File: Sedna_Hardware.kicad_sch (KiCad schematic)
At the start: 51 parts, among them J1 PJ-102A, J10 5-103735-2, J11 2-103634-9, J2 61201021721, J3 PPTC141LFBN-RC, J4 0878340619, J5 5-103634-2, J6 5-103361-1, J7 1935161, J8 1935161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

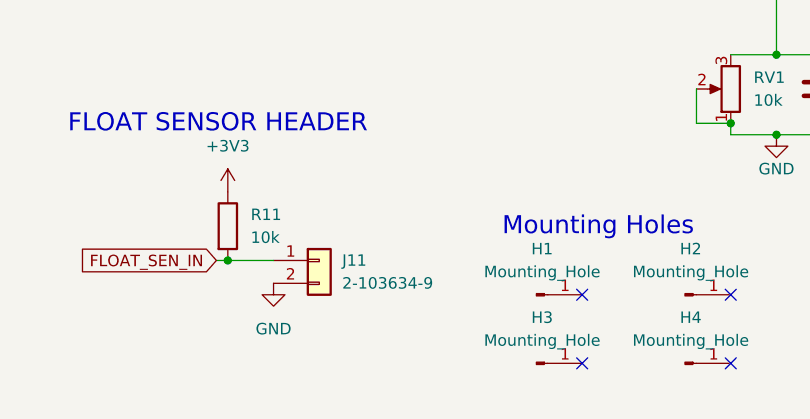
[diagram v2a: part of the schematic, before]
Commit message: placed new header's footpring
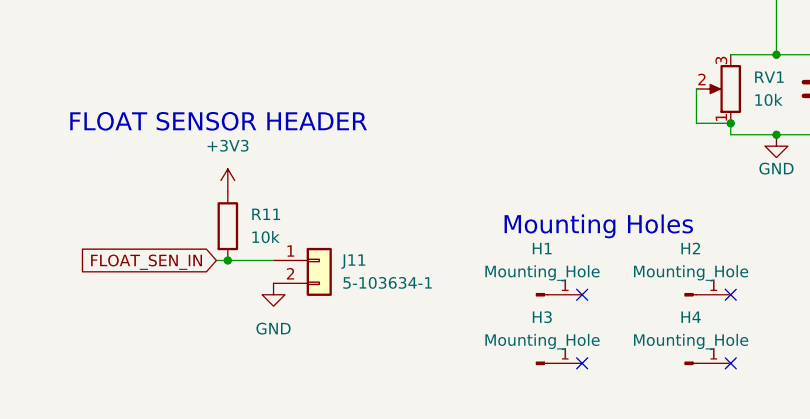
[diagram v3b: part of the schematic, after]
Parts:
- C12: DK_Datasheet_Link https://media.digikey.com/pdf/Data%20Sheets/Panasonic%20Ele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 -> https://www.nichicon.co.jp/english/products/pdfs/e-umt.pdf; DK_Detail_Page https://www.digikey.ca/en/products/detail/panasonic-electro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 -> https://www.digikey.ca/en/products/detail/nichicon/UMT0G470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; Digi-Key_PN P10417TB-ND -> 493-10267-1-ND; MPN ECA-1VM470I -> UMT0G470MDD1TP; Manufacturer Panasonic Electronic Components -> Nichicon
- J10: footprint 5-103634-2:TE_5-103634-2 -> 5-103735-2:MOLEX_1719740003
- J11: value 2-103634-9 -> 5-103634-1; footprint 2-644488-2:TE_2-644488-2 -> 2-103634-9:TE_2-103634-9; DK_Detail_Page https://www.digikey.ca/en/products/detail/te-connectivity-amp-connectors/2-103634-9/1889533 -> https://www.digikey.ca/en/products/detail/te-connectivity-amp-connectors/5-103634-1/1122421; Digi-Key_PN 2-103634-9-ND -> A33857-ND; MPN 2-103634-9 -> 5-103634-1
- J5, J9: footprint 2-644803-3:TE_2-644803-3 -> 5-103634-2:TE_5-103634-2
- J6: footprint 2-644488-3:TE_2-644488-3 -> 5-103361-1:TE_5-103361-1
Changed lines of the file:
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@@
       (effects (font (size 1.27 1.27)) (justify left))
     )
-    (property "Footprint" "2-644803-3:TE_2-644803-3" (id 2) (at 252.73 121.92 0)
+    (property "Footprint" "5-103634-2:TE_5-103634-2" (id 2) (at 252.73 121.92 0)
       (effects (font (size 1.27 1.27)) hide)
     )
@@
       (effects (font (size 1.27 1.27)) (justify left))
     )
-    (property "Value" "2-103634-9" (id 1) (at 109.22 181.6099 0)
-      (effects (font (size 1.27 1.27)) (justify left))
-    )
-    (property "Footprint" "2-644488-2:TE_2-644488-2" (id 2) (at 106.68 179.07 0)
+    (property "Value" "5-103634-1" (id 1) (at 109.22 181.6099 0)
+      (effects (font (size 1.27 1.27)) (justify left))
+    )
+    (property "Footprint" "2-103634-9:TE_2-103634-9" (id 2) (at 106.68 179.07 0)
       (effects (font (size 1.27 1.27)) hide)
     )
@@
       (effects (font (size 1.27 1.27)) hide)
     )
-    (property "Digi-Key_PN" "2-103634-9-ND" (id 4) (at 106.68 179.07 0)
-      (effects (font (size 1.27 1.27)) hide)
-    )
-    (property "MPN" "2-103634-9" (id 5) (at 106.68 179.07 0)
+    (property "Digi-Key_PN" "A33857-ND" (id 4) (at 106.68 179.07 0)
+      (effects (font (size 1.27 1.27)) hide)
+    )
+    (property "MPN" "5-103634-1" (id 5) (at 106.68 179.07 0)
       (effects (font (size 1.27 1.27)) hide)
     )
@@
       (effects (font (size 1.27 1.27)) hide)
     )
-    (property "DK_Detail_Page" "https://www.digikey.ca/en/products/detail/te-connectivity-amp-connectors/2-103634-9/1889533" (id 9) (at 106.68 179.07 0)
+    (property "DK_Detail_Page" "https://www.digikey.ca/en/products/detail/te-connectivity-amp-connectors/5-103634-1/1122421" (id 9) (at 106.68 179.07 0)
       (effects (font (size 1.27 1.27)) hide)
     )
@@
       (effects (font (size 1.27 1.27)) (justify left))
     )
-    (property "Footprint" "2-644803-3:TE_2-644803-3" (id 2) (at 251.46 152.4 0)
+    (property "Footprint" "5-103634-2:TE_5-103634-2" (id 2) (at 251.46 152.4 0)
       (effects (font (size 1.27 1.27)) hide)
     )
@@
     (property "Reference" "J6" (id 0) (at 147.32 116.84 0))
     (property "Value" "5-103361-1" (id 1) (at 147.32 119.38 0))
-    (property "Footprint" "2-644488-3:TE_2-644488-3" (id 2) (at 147.32 125.73 0)
+    (property "Footprint" "5-103361-1:TE_5-103361-1" (id 2) (at 147.32 125.73 0)
       (effects (font (size 1.27 1.27)) hide)
     )
@@
       (effects (font (size 1.27 1.27)) (justify left))
     )
-    (property "Footprint" "5-103634-2:TE_5-103634-2" (id 2) (at 53.34 177.8 0)
+    (property "Footprint" "5-103735-2:MOLEX_1719740003" (id 2) (at 53.34 177.8 0)
       (effects (font (size 1.27 1.27)) hide)
     )
@@
       (effects (font (size 1.27 1.27)) hide)
     )
-    (property "Datasheet" "https://media.digikey.com/pdf/Data%20Sheets/Panasonic%20Electronic%20Components/ECA-xxM%20Series,TypeA.pdf" (id 3) (at 220.98 153.67 0)
-      (effects (font (size 1.27 1.27)) hide)
-    )
-    (property "Digi-Key_PN" "P10417TB-ND" (id 4) (at 220.98 153.67 0)
-      (effects (font (size 1.27 1.27)) hide)
-    )
-    (property "MPN" "ECA-1VM470I" (id 5) (at 220.98 153.67 0)
+    (property "Datasheet" "https://www.nichicon.co.jp/english/products/pdfs/e-umt.pdf" (id 3) (at 220.98 153.67 0)
+      (effects (font (size 1.27 1.27)) hide)
+    )
+    (property "Digi-Key_PN" "493-10267-1-ND" (id 4) (at 220.98 153.67 0)
+      (effects (font (size 1.27 1.27)) hide)
+    )
+    (property "MPN" "UMT0G470MDD1TP" (id 5) (at 220.98 153.67 0)
       (effects (font (size 1.27 1.27)) hide)
     )
@@
       (effects (font (size 1.27 1.27)) hide)
     )
-    (property "DK_Datasheet_Link" "https://media.digikey.com/pdf/Data%20Sheets/Panasonic%20Electronic%20Components/ECA-xxM%20Series,TypeA.pdf" (id 7) (at 220.98 153.67 0)
-      (effects (font (size 1.27 1.27)) hide)
-    )
-    (property "DK_Detail_Page" "https://www.digikey.ca/en/products/detail/panasonic-electronic-components/ECA-1VM470I/268502" (id 8) (at 220.98 153.67 0)
-      (effects (font (size 1.27 1.27)) hide)
-    )
-    (property "Description" "CAP ALUM 47UF 20% 35V RADIAL" (id 9) (at 220.98 153.67 0)
-      (effects (font (size 1.27 1.27)) hide)
-    )
-    (property "Manufacturer" "Panasonic Electronic Components" (id 10) (at 220.98 153.67 0)
+    (property "DK_Datasheet_Link" "https://www.nichicon.co.jp/english/products/pdfs/e-umt.pdf" (id 7) (at 220.98 153.67 0)
+      (effects (font (size 1.27 1.27)) hide)
+    )
+    (property "DK_Detail_Page" "https://www.digikey.ca/en/products/detail/nichicon/UMT0G470MDD1TP/4312526" (id 8) (at 220.98 153.67 0)
+      (effects (font (size 1.27 1.27)) hide)
+    )
+    (property "Description" "47 µF 4 V Aluminum Electrolytic Capacitors Radial, Can - 1000 Hrs @ 105°C" (id 9) (at 220.98 153.67 0)
+      (effects (font (size 1.27 1.27)) hide)
+    )
+    (property "Manufacturer" "Nichicon" (id 10) (at 220.98 153.67 0)
       (effects (font (size 1.27 1.27)) hide)
     )
@@
     )
     (path "/2f024473-bb01-40b1-8417-7bc91aef9781"
-      (reference "J5") (unit 1) (value "5-103634-2") (footprint "2-644803-3:TE_2-644803-3")
+      (reference "J5") (unit 1) (value "5-103634-2") (footprint "5-103634-2:TE_5-103634-2")
     )
     (path "/475ad85a-f040-4464-8a55-a263ba5a9f31"
-      (reference "J6") (unit 1) (value "5-103361-1") (footprint "2-644488-3:TE_2-644488-3")
+      (reference "J6") (unit 1) (value "5-103361-1") (footprint "5-103361-1:TE_5-103361-1")
     )
     (path "/6291a5a5-163e-4b6a-943b-c26017563aff"
@@
     )
     (path "/3fd9f1df-2f2c-4bbd-af0b-d708b9312435"
-      (reference "J9") (unit 1) (value "5-103634-2") (footprint "2-644803-3:TE_2-644803-3")
+      (reference "J9") (unit 1) (value "5-103634-2") (footprint "5-103634-2:TE_5-103634-2")
     )
     (path "/d64a9bab-62fd-450b-bf60-da81d6cf8c9a"
-      (reference "J10") (unit 1) (value "5-103735-2") (footprint "5-103634-2:TE_5-103634-2")
+      (reference "J10") (unit 1) (value "5-103735-2") (footprint "5-103735-2:MOLEX_1719740003")
     )
     (path "/3048503d-6375-4b20-8607-4ec5ba50c92a"
-      (reference "J11") (unit 1) (value "2-103634-9") (footprint "2-644488-2:TE_2-644488-2")
+      (reference "J11") (unit 1) (value "5-103634-1") (footprint "2-103634-9:TE_2-103634-9")
     )
     (path "/1bbfbf59-e246-486c-9c83-59830ed0afbd"
